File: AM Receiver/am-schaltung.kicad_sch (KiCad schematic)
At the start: 71 parts, among them IC1 NE612AD, IC2 NE612AD, IC3 74HC74, IC4 TDA1072AT, IC5 74HTC4046, IC7 L78L05_SO8, P1 10k, P2 50k, P3 50k, Q1 MMBFJ310LT1G, Q2 MMBFJ310LT1G, Q3 BC547, Q4 BC547, Q5 BC557, U6 L78L08_SO8

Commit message: Finished PCB design for AM Receiver and fixed all remaining errors
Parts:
- added J100: Barrel_Jack_Switch, Connector_BarrelJack:BarrelJack_CUI_PJ-102AH_Horizontal, symbol Connector:Barrel_Jack_Switch
- added TP100: ANT_IN, TestPoint:TestPoint_Pad_D1.0mm, symbol Connector:TestPoint_Small
- added TP101: TP_VIN, TestPoint:TestPoint_Pad_D1.0mm, symbol Connector:TestPoint_Small
- added TP102: TP_GND, TestPoint:TestPoint_Pad_D1.0mm, symbol Connector:TestPoint_Small
- added TP103: TP_MIXER_IN, TestPoint:TestPoint_Pad_D1.0mm, symbol Connector:TestPoint_Small
- added TP104: TP_GND_RF, TestPoint:TestPoint_Pad_D1.0mm, symbol Connector:TestPoint_Small
- added TP105: TP_RF_MIXER_OUT, TestPoint:TestPoint_Pad_D1.0mm, symbol Connector:TestPoint_Small
- added TP106: TP_LO_MIXER_OUT, TestPoint:TestPoint_Pad_D1.0mm, symbol Connector:TestPoint_Small
- added TP107: TP_IF_FILTER_IN, TestPoint:TestPoint_Pad_D1.0mm, symbol Connector:TestPoint_Small
- added TP108: TP_DIV_OUT, TestPoint:TestPoint_Pad_D1.0mm, symbol Connector:TestPoint_Small
- added TP109: TP_GND_IF, TestPoint:TestPoint_Pad_D1.0mm, symbol Connector:TestPoint_Small
- added TP110: TP_IF_FILTER_OUT, TestPoint:TestPoint_Pad_D1.0mm, symbol Connector:TestPoint_Small
- added TP111: TP_VCO_OUT, TestPoint:TestPoint_Pad_D1.0mm, symbol Connector:TestPoint_Small
- added TP112: TP_8V, TestPoint:TestPoint_Pad_D1.0mm, symbol Connector:TestPoint_Small
- added TP113: TP_AUDIO_DEMOD, TestPoint:TestPoint_Pad_D1.0mm, symbol Connector:TestPoint_Small
- added TP114: TP_VCO_CTRL, TestPoint:TestPoint_Pad_D1.0mm, symbol Connector:TestPoint_Small
- added TP115: TP_AUDIO_DRV, TestPoint:TestPoint_Pad_D1.0mm, symbol Connector:TestPoint_Small
- added TP116: TP_5V, TestPoint:TestPoint_Pad_D1.0mm, symbol Connector:TestPoint_Small
- added TP117: TP_SPK_OUT, TestPoint:TestPoint_Pad_D1.0mm, symbol Connector:TestPoint_Small
- AE100: renamed from AE1; symbol Custom_Device:Antenna -> Device:Antenna_Loop
- C100: renamed from C1; manf# (none) -> CC0603JRNPO9BN470
- C101: renamed from C2; manf# (none) -> C0603C104K5RACTU
- C102: renamed from C3; manf# (none) -> C0603C104K5RACTU
- C103: renamed from C4; manf# (none) -> C0603C101J5GACTU
- C104: renamed from C5; symbol Custom_Device:C -> Device:C; manf# (none) -> C0603C104K5RACTU
- C105: renamed from C6; symbol Custom_Device:C -> Device:C; manf# (none) -> C0603C104K5RACTU
- C106: renamed from C7; manf# (none) -> C0603C104K5RACTU
- C107: renamed from C8; manf# (none) -> C0603C104K5RACTU
- C108: renamed from C9; manf# (none) -> C0603C104K5RACTU
- C109: renamed from C10; manf# (none) -> C0603C104K5RACTU
- C110: renamed from C11; manf# (none) -> C0603C104K5RACTU
- C111: renamed from C12; symbol Custom_Device:C -> Device:C; manf# (none) -> C0603C104K5RACTU
- C112: renamed from C13; manf# (none) -> C0603C271J5GACTU
- C113: renamed from C14; value 100p -> 7–100p; footprint Capacitor_SMD:C_0603_1608Metric_Pad1.08x0.95mm_HandSolder -> AM_Radio:Vishay_BFC280907015_Trimmer_7-100pF; manf# (none) -> BFC280907015
- C114: renamed from C15; symbol Custom_Device:C -> Device:C; manf# (none) -> C0603C104K5RACTU
- C115: renamed from C16; manf# (none) -> C0603C101J5GACTU
- C116: renamed from C17; manf# (none) -> C0603C104K5RACTU
- C117: renamed from C18; symbol Custom_Device:C_Small -> Device:C_Small; manf# (none) -> CC0603JRNPO9BN470
- C118: renamed from C19; manf# (none) -> C0603C104K5RACTU
- C119: renamed from C20; manf# (none) -> C0603C391J5GACTU
- C120: renamed from C21; value 100p -> 7–100p; footprint Capacitor_SMD:C_0603_1608Metric_Pad1.08x0.95mm_HandSolder -> AM_Radio:Vishay_BFC280907015_Trimmer_7-100pF; manf# (none) -> BFC280907015
- C121: renamed from C22; manf# (none) -> C0603C104K5RACTU
- C122: renamed from C23; footprint Capacitor_SMD:C_0603_1608Metric_Pad1.08x0.95mm_HandSolder -> Capacitor_Tantalum_SMD:CP_EIA-3216-18_Kemet-A_HandSolder; symbol Custom_Device:C_Polarized -> Device:C_Polarized; manf# (none) -> F931E225KAA
- C123: renamed from C24; footprint Capacitor_SMD:C_0603_1608Metric_Pad1.08x0.95mm_HandSolder -> Capacitor_Tantalum_SMD:CP_EIA-3528-21_Kemet-B_HandSolder; symbol Custom_Device:C_Polarized -> Device:C_Polarized; manf# (none) -> TCJB226M025R0150
- C124: renamed from C25; manf# (none) -> GRM188R71H224KAC4D
- C125: renamed from C26; manf# (none) -> C0603C104K5RACTU
- C126: renamed from C27; manf# (none) -> CL10B103KB8NNNC
- C127: renamed from C28; symbol Custom_Device:C -> Device:C; manf# (none) -> C0603C104K5RACTU
- C128: renamed from C29; manf# (none) -> C0603C104K5RACTU
- C129: renamed from C30; symbol Custom_Device:C -> Device:C; manf# (none) -> C0603C104K5RACTU
- C130: renamed from C31; manf# (none) -> C0603C104K5RACTU
- C131: renamed from C32; footprint Capacitor_SMD:C_0603_1608Metric_Pad1.08x0.95mm_HandSolder -> Capacitor_Tantalum_SMD:CP_EIA-7343-20_Kemet-V_HandSolder; symbol Custom_Device:C_Polarized -> Device:C_Polarized; manf# (none) -> TCJY476M025R0100E
- C132: renamed from C33; footprint Capacitor_SMD:C_0603_1608Metric_Pad1.08x0.95mm_HandSolder -> Capacitor_SMD:CP_Elec_10x10.5; symbol Custom_Device:C_Polarized -> Device:C_Polarized; manf# (none) -> EMZA250ARA471MJA0G
- C133: renamed from C34; manf# (none) -> C0603C104K5RACTU
- D100: renamed from D1; footprint Diode_THT:D_DO-35_SOD27_P7.62mm_Horizontal -> Diode_SMD:D_SOD-123; manf# (none) -> 1N4148W-7-F
- D101: renamed from D2; footprint Diode_THT:D_DO-35_SOD27_P7.62mm_Horizontal -> Diode_SMD:D_SOD-123; manf# (none) -> 1N4148W-7-F
- FL100: renamed from FL1; value (none) -> SFZ455A; footprint (none) -> AM_Radio:SFZ455A; symbol AM_Receiver:SFD455 -> AM_Receiver:SFZ455A; manf# (none) -> SFZ455A
- IC100: renamed from IC1; value NE612AD -> SA612AD; symbol AM_Receiver:NE612AD -> AM_Receiver:NE612AD / SA612AD; MPN (none) -> SA612AD/01,118; manf# (none) -> SA612AD
- IC101: renamed from IC2; value NE612AD -> SA612AD; symbol AM_Receiver:NE612AD -> AM_Receiver:NE612AD / SA612AD; MPN (none) -> SA612AD/01,118; manf# (none) -> SA612AD
- IC102: renamed from IC3; value 74HC74 -> 74HC74D; manf# (none) -> 74HC74D,653
- IC103: renamed from IC4; symbol AM_Receiver:TDA1072 -> AM_Receiver:TDA1072AT; MPN (none) -> TDA1072AT/V4,112; manf# (none) -> TDA1072AT
- IC104: renamed from IC5; value 74HTC4046 -> 74HCT4046AD; symbol AM_Receiver:74HTC4046 -> AM_Receiver:74HCT4046AD; MPN (none) -> 74HCT4046AD; manf# (none) -> 74HCT4046A
- IC105: renamed from U6; manf# (none) -> L78L08ACD13TR
- IC106: renamed from IC7; manf# (none) -> L78L05ACD13TR
- L100: renamed from L1; footprint Inductor_SMD:L_0201_0603Metric_Pad0.64x0.40mm_HandSolder -> Inductor_SMD:L_1812_4532Metric_Pad1.30x3.40mm_HandSolder; symbol Custom_Device:L -> Device:L; manf# (none) -> CC453232-181KL
- LS100: renamed from LS1; footprint (none) -> TerminalBlock_Phoenix:TerminalBlock_Phoenix_MKDS-1,5-2-5.08_1x02_P5.08mm_Horizontal; manf# (none) -> 1715721
- P100: renamed from P1; footprint Potentiometer_SMD:Potentiometer_Bourns_3224W_Vertical -> Potentiometer_SMD:Potentiometer_Bourns_TC33X_Vertical; symbol Custom_Device:R_Potentiometer -> Device:R_Potentiometer; manf# (none) -> TC33X-2-103E
- P101: renamed from P2; footprint Potentiometer_SMD:Potentiometer_Bourns_3224W_Vertical -> Potentiometer_THT:Potentiometer_Bourns_3386P_Vertical; symbol Custom_Device:R_Potentiometer -> Device:R_Potentiometer; manf# (none) -> 3386P-1-503LF
- P102: renamed from P3; footprint Potentiometer_SMD:Potentiometer_Bourns_3224W_Vertical -> Potentiometer_THT:Potentiometer_Bourns_3386P_Vertical; symbol Custom_Device:R_Potentiometer -> Device:R_Potentiometer; manf# (none) -> 3386P-1-503LF
- Q100: renamed from Q1; value MMBFJ310LT1G -> MMBFJ310LT3G; footprint Package_TO_SOT_SMD:SOT-23 -> Package_TO_SOT_SMD:SOT-23_Handsoldering; manf# (none) -> MMBFJ310LT3G
- Q101: renamed from Q2; value MMBFJ310LT1G -> MMBFJ310LT3G; footprint Package_TO_SOT_SMD:SOT-23 -> Package_TO_SOT_SMD:SOT-23_Handsoldering; manf# (none) -> MMBFJ310LT3G
- Q102: renamed from Q3; footprint Package_TO_SOT_SMD:SOT-23 -> Package_TO_SOT_THT:TO-92_HandSolder; manf# (none) -> BC547BBU
- Q103: renamed from Q4; footprint Package_TO_SOT_SMD:SOT-23 -> Package_TO_SOT_THT:TO-92_HandSolder; manf# (none) -> BC547BBU
- Q104: renamed from Q5; footprint Package_TO_SOT_SMD:SOT-23 -> Package_TO_SOT_THT:TO-92_HandSolder; manf# (none) -> BC557BTA
- R100: renamed from R1; manf# (none) -> RC0603FR-071ML
- R101: renamed from R2; manf# (none) -> RC0603FR-071KL
- R102: renamed from R3; manf# (none) -> RC0603FR-071KL
- R103: renamed from R4; manf# (none) -> RC0603FR-071K5L
- R104: renamed from R5; manf# (none) -> RC0603FR-071K5L
- R105: renamed from R6; symbol Custom_Device:R -> Device:R; manf# (none) -> RC0603FR-0722KL
- R106: renamed from R7; symbol Custom_Device:R -> Device:R; manf# (none) -> RC0603FR-0722KL
- R107: renamed from R8; manf# (none) -> RC0603FR-07470KL
- R108: renamed from R9; manf# (none) -> RC0603FR-072K2L
- R109: renamed from R10; manf# (none) -> RC0603FR-072K2L
- R110: renamed from R11; manf# (none) -> RC0603FR-073K9L
- R111: renamed from R12; manf# (none) -> RC0603FR-0715KL
- R112: renamed from R13; manf# (none) -> RC0603FR-0715KL
- R113: renamed from R14; symbol Custom_Device:R -> Device:R; manf# (none) -> RC0603FR-071M5L
- R114: renamed from R15; manf# (none) -> RC0603FR-074K7L
- R115: renamed from R16; manf# (none) -> RC0603FR-07100RL
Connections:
- net +12V ...+15V: now also J100.1, TP101.1
- net +5V: now also TP116.1
- net +8V: now also TP112.1
- net GND: now also AE100.1, FL100.2, FL100.5, J100.2, J100.3, TP102.1, TP104.1, TP109.1; no longer FL100.3
- net at C112.1, IC100.4 (OUTA), P100.1: now also TP105.1
- net at C131.2, LS100.1: now also TP117.1
- net at C129.1, Q102.2 (B), R113.2: now also TP115.1
- net at C104.1, IC100.1 (INA): now also TP103.1
- net at C128.1, IC104.9 (VCO_IN), P102.2: now also TP114.1
- net at IC102.2 (D), IC102.9 (Q), R106.1: now also TP108.1
- net at FL100.1, Q101.2 (D), R108.2: now also TP107.1
- net at C117.2: now also FL100.3; no longer FL100.1
- net at C117.1: now also FL100.4; no longer FL100.2
- net at IC103.3: now also FL100.6, TP110.1; no longer FL100.2
- net at C127.1, P101.1: now also TP113.1
- net at C113.2, IC101.5 (OUTB): now also TP106.1
- net at IC102.11 (C), IC104.3 (COMP_IN), IC104.4 (VCO_Out): now also TP111.1
- net at L100.2: now also AE100.2, TP100.1; no longer AE100.1 (A)
- no-connect marks 0 -> 17
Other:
- title: AM-Receiver -> AM Receiver
- moved on the sheet: AE100, C104, C117, C120, C125, C131, IC102B, L100, LS100, R104, R108

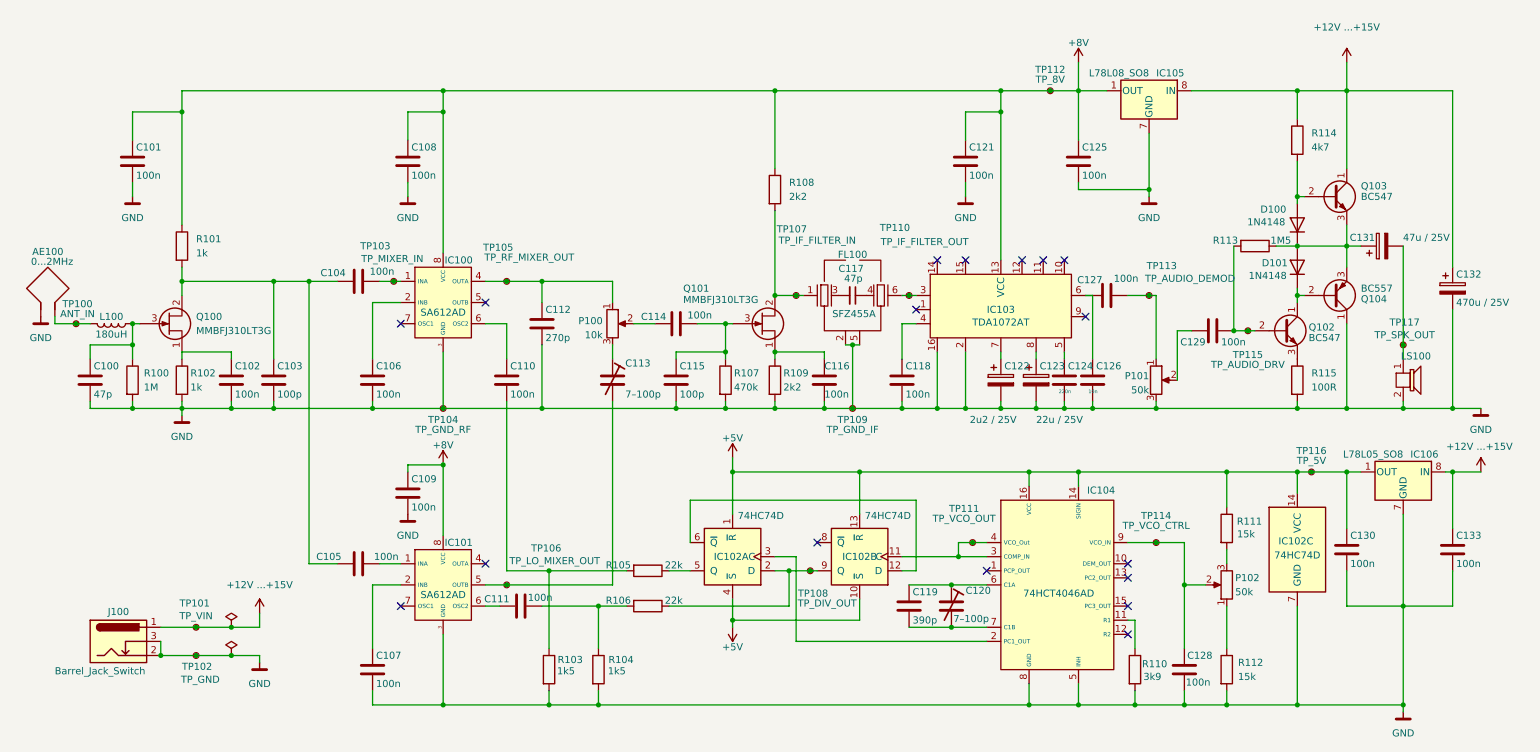
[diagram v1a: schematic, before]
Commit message: Updated values of all resistors and capacitors
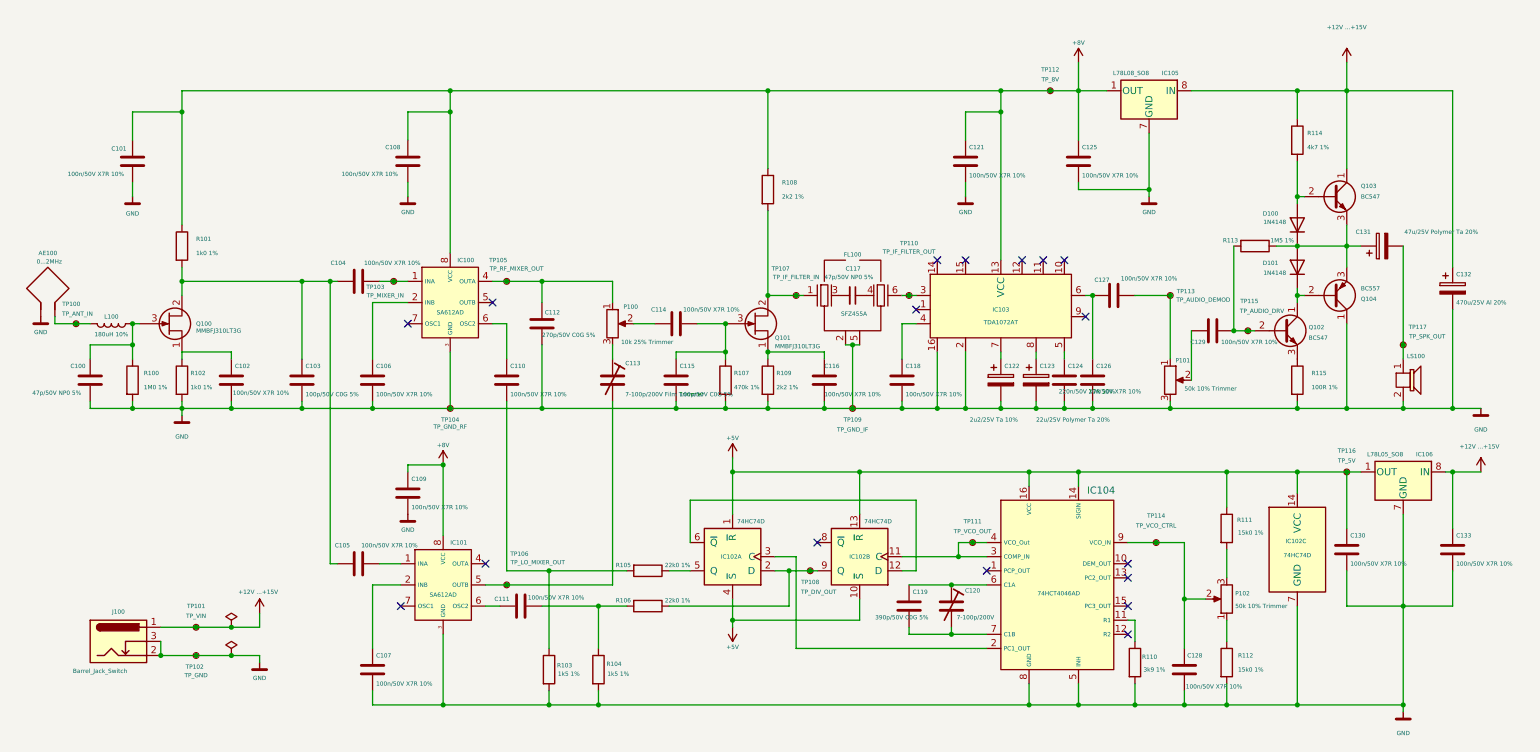
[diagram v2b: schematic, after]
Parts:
- C100, C117: value 47p -> 47p/50V NP0 5%
- C101, C102, C104, C105, C106, C107, C108, C109, C110, C111, C114, C116, C118, C121, C125, C127, C128, C129, C130, C133: value 100n -> 100n/50V X7R 10%
- C103, C115: value 100p -> 100p/50V C0G 5%
- C112: value 270p -> 270p/50V C0G 5%
- C113: value 7–100p -> 7-100p/200V Film Trimmer
- C119: value 390p -> 390p/50V C0G 5%
- C120: value 7–100p -> 7-100p/200V
- C122: value 2u2 / 25V -> 2u2/25V Ta 10%
- C123: value 22u / 25V -> 22u/25V Polymer Ta 20%
- C124: value 220n -> 220n/50V X7R 10%
- C126: value 10n -> 10n/50V X7R 10%
- C131: value 47u / 25V -> 47u/25V Polymer Ta 20%
- C132: value 470u / 25V -> 470u/25V Al 20%
- L100: value 180uH -> 180uH 10%
- P100: value 10k -> 10k 25% Trimmer
- P101, P102: value 50k -> 50k 10% Trimmer
- R100: value 1M -> 1M0 1%
- R101, R102: value 1k -> 1k0 1%
- R103, R104: value 1k5 -> 1k5 1%
- R105, R106: value 22k -> 22k0 1%
- R107: value 470k -> 470k 1%
- R108, R109: value 2k2 -> 2k2 1%
- R110: value 3k9 -> 3k9 1%
- R111, R112: value 15k -> 15k0 1%
- R113: value 1M5 -> 1M5 1%
- R114: value 4k7 -> 4k7 1%
- R115: value 100R -> 100R 1%
- TP100: value ANT_IN -> TP_ANT_IN
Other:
- moved on the sheet: C103, C127, IC100, P101, P102, Q101, R108, R109, R110, R112, TP104, TP113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

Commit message: updated some remaining issues one the PCB
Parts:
- C113: value 7-100p/200V Film Trimmer -> 7-100p/200V
- IC104: manf# 74HCT4046A -> 74HCT4046AD
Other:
- moved on the sheet: C112, C113, C115, P100

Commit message: Updated Schematic to use multiple sheets and repaired PCB
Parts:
- removed C105, C107, C109, C111, C125, C128, C129, C130, C133: 100n/50V X7R 10%, Capacitor_SMD:C_0603_1608Metric_Pad1.08x0.95mm_HandSolder, symbol Device:C
- removed C119: 390p/50V C0G 5%, Capacitor_SMD:C_0603_1608Metric_Pad1.08x0.95mm_HandSolder, symbol Device:C
- removed C120: 7-100p/200V, AM_Radio:Vishay_BFC280907015_Trimmer_7-100pF, symbol Device:C_Trim
- removed C131: 47u/25V Polymer Ta 20%, Capacitor_Tantalum_SMD:CP_EIA-7343-20_Kemet-V_HandSolder, symbol Device:C_Polarized
- removed C132: 470u/25V Al 20%, Capacitor_SMD:CP_Elec_10x10.5, symbol Device:C_Polarized
- removed D100, D101: 1N4148, Diode_SMD:D_SOD-123, symbol Diode:1N4148
- removed IC101: SA612AD, Package_SO:SOIC-8_3.9x4.9mm_P1.27mm, symbol AM_Receiver:NE612AD / SA612AD
- removed IC102: 74HC74D, Package_SO:SOIC-14_3.9x8.7mm_P1.27mm, symbol 74xx:74HC74
- removed IC104: 74HCT4046AD, Package_SO:SOIC-16_3.9x9.9mm_P1.27mm, symbol AM_Receiver:74HCT4046AD
- removed IC105: L78L08_SO8, Package_SO:SOIC-8_3.9x4.9mm_P1.27mm, symbol Regulator_Linear:L78L08_SO8
- removed IC106: L78L05_SO8, Package_SO:SOIC-8_3.9x4.9mm_P1.27mm, symbol Regulator_Linear:L78L05_SO8
- removed J100: Barrel_Jack_Switch, Connector_BarrelJack:BarrelJack_CUI_PJ-102AH_Horizontal, symbol Connector:Barrel_Jack_Switch
- removed LS100: (no value), TerminalBlock_Phoenix:TerminalBlock_Phoenix_MKDS-1,5-2-5.08_1x02_P5.08mm_Horizontal, symbol AM_Receiver:LS
- removed P101, P102: 50k 10% Trimmer, Potentiometer_THT:Potentiometer_Bourns_3386P_Vertical, symbol Device:R_Potentiometer
- removed Q102, Q103: BC547, Package_TO_SOT_THT:TO-92_HandSolder, symbol Transistor_BJT:BC547
- removed Q104: BC557, Package_TO_SOT_THT:TO-92_HandSolder, symbol Transistor_BJT:BC557
- removed R103, R104: 1k5 1%, Resistor_SMD:R_0603_1608Metric_Pad0.98x0.95mm_HandSolder, symbol Device:R
- removed R105, R106: 22k0 1%, Resistor_SMD:R_0603_1608Metric_Pad0.98x0.95mm_HandSolder, symbol Device:R
- removed R110: 3k9 1%, Resistor_SMD:R_0603_1608Metric_Pad0.98x0.95mm_HandSolder, symbol Device:R
- removed R111, R112: 15k0 1%, Resistor_SMD:R_0603_1608Metric_Pad0.98x0.95mm_HandSolder, symbol Device:R
- removed R113: 1M5 1%, Resistor_SMD:R_0603_1608Metric_Pad0.98x0.95mm_HandSolder, symbol Device:R
- removed R114: 4k7 1%, Resistor_SMD:R_0603_1608Metric_Pad0.98x0.95mm_HandSolder, symbol Device:R
- removed R115: 100R 1%, Resistor_SMD:R_0603_1608Metric_Pad0.98x0.95mm_HandSolder, symbol Device:R
- removed TP101: TP_VIN, TestPoint:TestPoint_Pad_D1.0mm, symbol Connector:TestPoint_Small
- removed TP102: TP_GND, TestPoint:TestPoint_Pad_D1.0mm, symbol Connector:TestPoint_Small
- removed TP106: TP_LO_MIXER_OUT, TestPoint:TestPoint_Pad_D1.0mm, symbol Connector:TestPoint_Small
- removed TP108: TP_DIV_OUT, TestPoint:TestPoint_Pad_D1.0mm, symbol Connector:TestPoint_Small
- removed TP111: TP_VCO_OUT, TestPoint:TestPoint_Pad_D1.0mm, symbol Connector:TestPoint_Small
- removed TP112: TP_8V, TestPoint:TestPoint_Pad_D1.0mm, symbol Connector:TestPoint_Small
- removed TP114: TP_VCO_CTRL, TestPoint:TestPoint_Pad_D1.0mm, symbol Connector:TestPoint_Small
- removed TP115: TP_AUDIO_DRV, TestPoint:TestPoint_Pad_D1.0mm, symbol Connector:TestPoint_Small
- removed TP116: TP_5V, TestPoint:TestPoint_Pad_D1.0mm, symbol Connector:TestPoint_Small
- removed TP117: TP_SPK_OUT, TestPoint:TestPoint_Pad_D1.0mm, symbol Connector:TestPoint_Small
- FL100: manf# SFZ455A -> SFZLA455KN2A-B0
- IC100: MPN SA612AD/01,118 -> (none); manf# SA612AD -> SA612AD/01,118
- IC103: MPN TDA1072AT/V4,112 -> (none); ProcurementNote (none) -> Exact legacy manf# TDA1072AT/V4,112; use SOIC-16 package on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; manf# TDA1072AT -> TDA1072AT/V4,112
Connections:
- net RF_MIXER_OUT: now reaches C110.2
- net RF_AMP_OUT: now reaches C103.1, C104.2, Q100.2 (D), R101.2
- net Audio_Out: now reaches C127.1, TP113.1
- net RF_TANK_LOW: now reaches C113.2
- no-connect marks 17 -> 9
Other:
- moved on the sheet: AE100, C100, C101, C102, C103, C104, C106, C108, C110, C112, C113, C114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

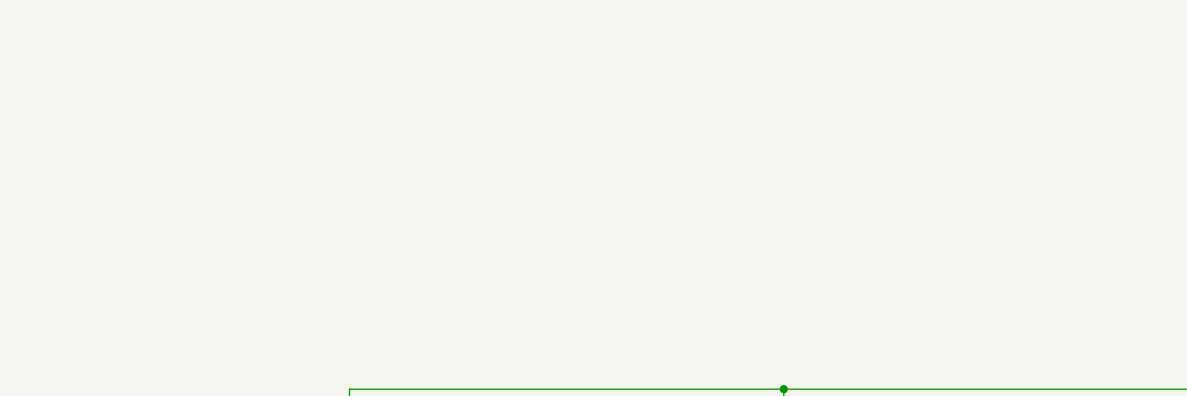
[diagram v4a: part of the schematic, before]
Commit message: Filled out information in User.Drawings on PCB
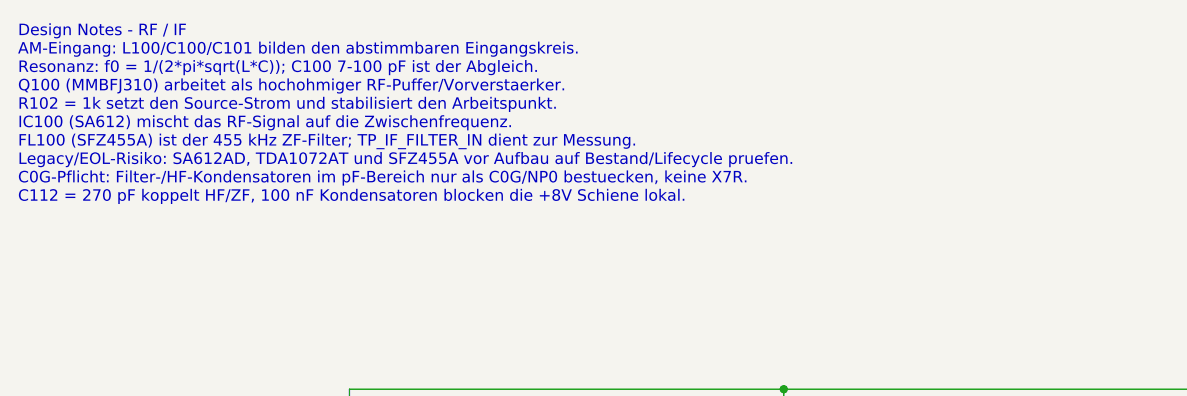
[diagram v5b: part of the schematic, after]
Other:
- note added: "Design Notes - RF / IF AM-Eingang: L100/C100/C101 bilden den abstimmbaren Eingangskreis. Resonanz: f0 = 1/(2*pi*sqrt(L*C)); C100 7-100 pF ist der Abgleich. Q100 (MMBFJ310) arbeitet als hochohmiger RF-Puffer/Vorverstaerker. R102 = 1k setzt den Source-Strom und stabilisiert den Arbeitspunkt. IC100 (SA612) mischt das RF-Signal auf die Zwischenfrequenz. FL100 (SFZ455A) ist der 455 kHz ZF-Filter; TP_I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"
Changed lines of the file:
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@@
 		(comment 3 "T. Brown")
+	)
+	(text "Design Notes - RF / IF\nAM-Eingang: L100/C100/C101 bilden den abstimmbaren Eingangskreis.\nResonanz: f0 = 1/(2*pi*sqrt(L*C)); C100 7-100 pF ist der Abgleich.\nQ100 (MMBFJ310) arbeitet als hochohmiger RF-Puffer/Vorverstaerker.\nR102 = 1k setzt den Source-Strom und stabilisiert den Arbeitspunkt.\nIC100 (SA612) mischt das RF-Signal auf die Zwischenfrequenz.\nFL100 (SFZ455A) ist der 455 kHz ZF-Filter; TP_IF_FILTER_IN dient zur Messung.\nLegacy/EOL-Risiko: SA612AD, TDA1072AT und SFZ455A vor Aufbau auf Bestand/Lifecycle pruefen.\nC0G-Pflicht: Filter-/HF-Kondensatoren im pF-Bereich nur als C0G/NP0 bestuecken, keine X7R.\nC112 = 270 pF koppelt HF/ZF, 100 nF Kondensatoren blocken die +8V Schiene lokal."
+		(exclude_from_sim no)
+		(at 35.56 34.29 0)
+		(effects
+			(font
+				(size 1.27 1.27)
+			)
+			(justify left)
+		)
 	)
 	(junction

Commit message: Updated User.drawing information and Design Review
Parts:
- FL100: ProcurementNote (none) -> Legacy/EOL risk for SFZ455A/SFZLA455KN2A-B0; verify stock/l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
- IC100: ProcurementNote (none) -> Legacy/EOL risk for SA612AD/01,118; verify stock/lifecycle 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
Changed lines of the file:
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@@
+			)
+		)
+		(property "ProcurementNote" "Legacy/EOL risk for SA612AD/01,118; verify stock/lifecycle and approved substitute before build."
+			(at 120.65 102.87 0)
+			(hide yes)
+			(show_name no)
+			(do_not_autoplace no)
+			(effects
+				(font
+					(size 1.27 1.27)
+				)
 			)
 		)
@@
 			(at 193.04 101.6 0)
 			(hide yes)
+			(show_name no)
+			(do_not_autoplace no)
+			(effects
+				(font
+					(size 1.27 1.27)
+				)
+			)
+		)
+		(property "ProcurementNote" "Legacy/EOL risk for SFZ455A/SFZLA455KN2A-B0; verify stock/lifecycle or compatible 455 kHz ceramic IF filter before build."
+			(at 193.04 101.6 0)
+			(hide yes)
